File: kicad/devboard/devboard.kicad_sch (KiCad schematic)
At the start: 35 parts, among them J1 USB_C_Receptacle, J2 Conn_01x04_Socket, J3 Conn_02x03_Top_Bottom, J4 Conn_02x02_Top_Bottom, U1 LM3940, U2 CH340G, U3 STM32G030K8Tx, Y1 12 MHz, Y2 8 MHz

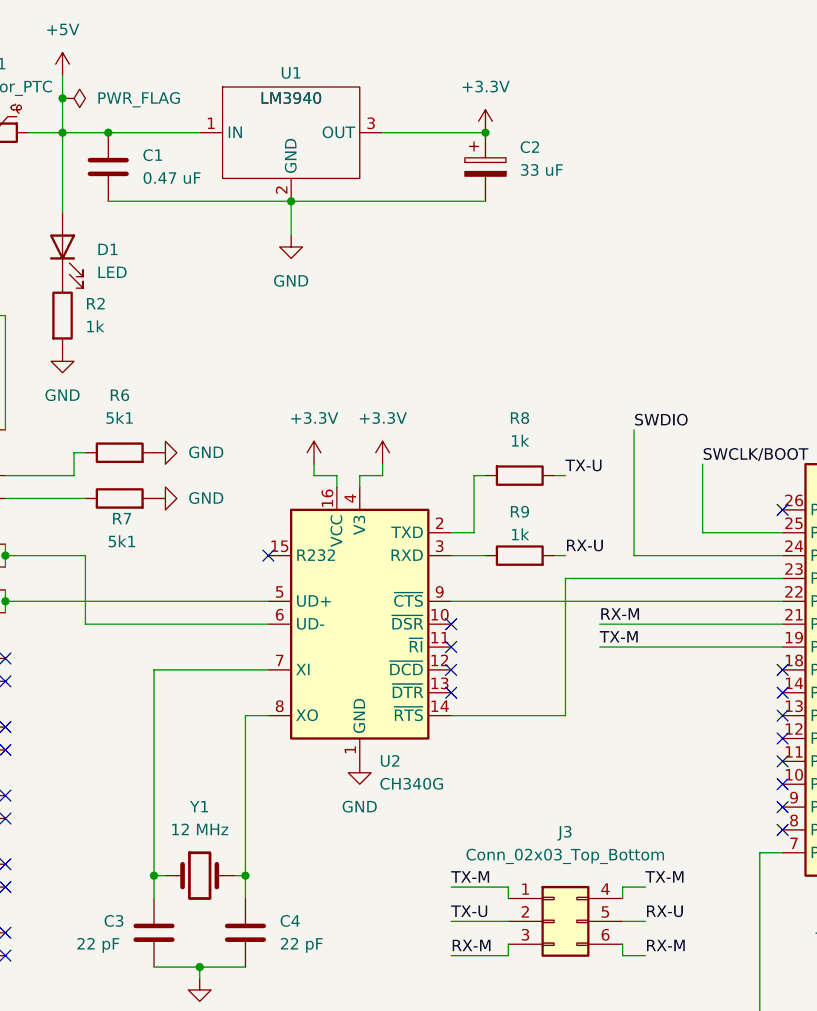
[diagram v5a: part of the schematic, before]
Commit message: updated footprints for Y1, C2
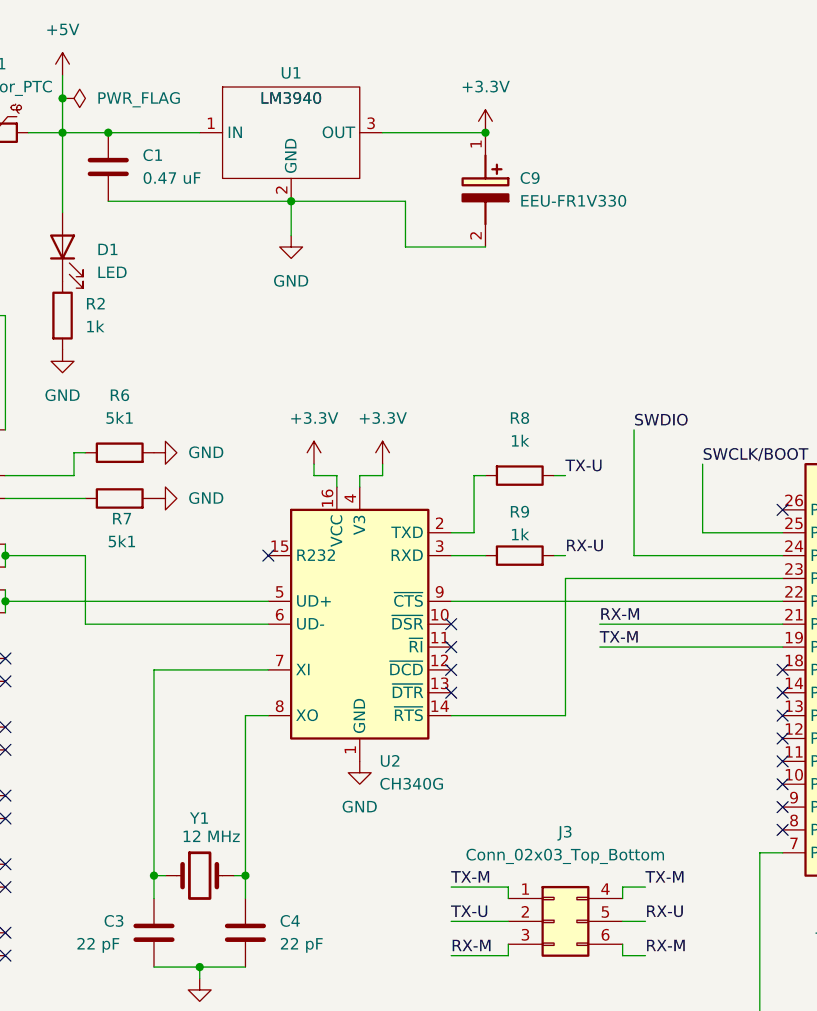
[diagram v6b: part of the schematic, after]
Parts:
- removed C2: 33 uF, Capacitor_SMD:C_0603_1608Metric, symbol Device:C_Polarized
- added C9: EEU-FR1V330, mesonlib:EEU-FR1330, symbol mesonlib:EEU-FR1V330
- Y1: footprint Resistor_SMD:R_0603_1608Metric -> Crystal:Crystal_SMD_HC49-SD
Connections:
- net +3.3V: now also C9.1 (+)
- net GND: now also C9.2 (-)
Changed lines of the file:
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@@
 	)
 	(junction
+		(at 97.79 31.75)
+		(diameter 0)
+		(color 0 0 0 0)
+	)
+	(junction
 		(at 60.96 114.3)
 		(diameter 0)
@@
 	)
 	(junction
-		(at 97.79 31.75)
-		(diameter 0)
-		(color 0 0 0 0)
-	)
-	(junction
 		(at 71.12 114.3)
 		(diameter 0)
@@
 	(wire
 		(pts
+			(xy 88.9 44.45) (xy 88.9 39.37)
+		)
+		(stroke
+			(width 0)
+			(type default)
+		)
+	)
+	(wire
+		(pts
 			(xy 66.04 124.46) (xy 71.12 124.46)
 		)
@@
 	(wire
 		(pts
+			(xy 97.79 44.45) (xy 88.9 44.45)
+		)
+		(stroke
+			(width 0)
+			(type default)
+		)
+	)
+	(wire
+		(pts
 			(xy 78.74 69.85) (xy 81.28 69.85)
 		)
@@
 	(wire
 		(pts
-			(xy 76.2 39.37) (xy 97.79 39.37)
+			(xy 231.14 101.6) (xy 237.49 101.6)
 		)
 		(stroke
@@
 	(wire
 		(pts
-			(xy 231.14 101.6) (xy 237.49 101.6)
+			(xy 39.37 31.75) (xy 39.37 52.07)
 		)
 		(stroke
@@
 	(wire
 		(pts
-			(xy 39.37 31.75) (xy 39.37 52.07)
+			(xy 44.45 82.55) (xy 44.45 83.82)
 		)
 		(stroke
@@
 	(wire
 		(pts
-			(xy 44.45 82.55) (xy 44.45 83.82)
+			(xy 55.88 39.37) (xy 76.2 39.37)
 		)
 		(stroke
@@
 	(wire
 		(pts
-			(xy 55.88 39.37) (xy 76.2 39.37)
+			(xy 50.8 31.75) (xy 50.8 40.64)
 		)
 		(stroke
@@
 	(wire
 		(pts
-			(xy 50.8 31.75) (xy 50.8 40.64)
+			(xy 60.96 114.3) (xy 62.23 114.3)
 		)
 		(stroke
@@
 	(wire
 		(pts
-			(xy 60.96 114.3) (xy 62.23 114.3)
+			(xy 143.51 116.84) (xy 143.51 120.65)
 		)
 		(stroke
@@
 	(wire
 		(pts
-			(xy 143.51 116.84) (xy 143.51 120.65)
+			(xy 76.2 39.37) (xy 88.9 39.37)
 		)
 		(stroke
@@
 	)
 	(symbol
-		(lib_id "Device:C_Polarized")
-		(at 97.79 35.56 0)
-		(unit 1)
-		(exclude_from_sim no)
-		(in_bom yes)
-		(on_board yes)
-		(dnp no)
-		(fields_autoplaced yes)
-		(property "Reference" "C2"
-			(at 101.6 33.4009 0)
-			(effects
-				(font
-					(size 1.27 1.27)
-				)
-				(justify left)
-			)
-		)
-		(property "Value" "33 uF"
-			(at 101.6 35.9409 0)
-			(effects
-				(font
-					(size 1.27 1.27)
-				)
-				(justify left)
-			)
-		)
-		(property "Footprint" "Capacitor_SMD:C_0603_1608Metric"
-			(at 98.7552 39.37 0)
-			(effects
-				(font
-					(size 1.27 1.27)
-				)
-				(hide yes)
-			)
-		)
-		(property "Datasheet" "~"
-			(at 97.79 35.56 0)
-			(effects
-				(font
-					(size 1.27 1.27)
-				)
-				(hide yes)
-			)
-		)
-		(property "Description" "Polarized capacitor"
-			(at 97.79 35.56 0)
-			(effects
-				(font
-					(size 1.27 1.27)
-				)
-				(hide yes)
-			)
-		)
-		(pin "1"
-		)
-		(pin "2"
-		)
-		(instances
-			(project "devboard"
-				(path "/c3bd2aeb-acec-4e93-ab92-7a030f22ab8b"
-					(reference "C2")
-					(unit 1)
-				)
-			)
-		)
-	)
-	(symbol
 		(lib_id "power:PWR_FLAG")
 		(at 50.8 27.94 270)
@@
 		(on_board yes)
 		(dnp no)
-		(fields_autoplaced yes)
 		(property "Reference" "Y1"
-			(at 66.04 106.68 0)
+			(at 66.04 107.95 0)
 			(effects
 				(font
@@
 		)
 		(property "Value" "12 MHz	"
-			(at 66.04 109.22 0)
+			(at 67.31 109.982 0)
 			(effects
 				(font
@@
 			)
 		)
-		(property "Footprint" "Resistor_SMD:R_0603_1608Metric"
+		(property "Footprint" "Crystal:Crystal_SMD_HC49-SD"
 			(at 66.04 114.3 0)
 			(effects
@@
 					(unit 1)
 				)
+			)
+		)
+	)
+	(symbol
+		(lib_id "mesonlib:EEU-FR1V330")
+		(at 97.79 31.75 270)
+		(unit 1)
+		(exclude_from_sim no)
+		(in_bom yes)
+		(on_board yes)
+		(dnp no)
+		(fields_autoplaced yes)
+		(property "Reference" "C9"
+			(at 101.6 36.8299 90)
+			(effects
+				(font
+					(size 1.27 1.27)
+				)
+				(justify left)
+			)
+		)
+		(property "Value" "EEU-FR1V330"
+			(at 101.6 39.3699 90)
+			(effects
+				(font
+					(size 1.27 1.27)
+				)
+				(justify left)
+			)
+		)
+		(property "Footprint" "mesonlib:EEU-FR1330"
+			(at 1.6 40.64 0)
+			(effects
+				(font
+					(size 1.27 1.27)
+				)
+				(justify left top)
+				(hide yes)
+			)
+		)
+		(property "Datasheet" "http://industrial.panasonic.com/cdbs/www-data/pdf/RDF0000/ABA0000C1259.pdf"
+			(at -98.4 40.64 0)
+			(effects
+				(font
+					(size 1.27 1.27)
+				)
+				(justify left top)
+				(hide yes)
+			)
+		)
+		(property "Description" "Aluminium Electrolytic Capacitor, Radial Lead Type, 105C,  33UF 20% 35V RADIAL"
+			(at 97.79 31.75 0)
+			(effects
+				(font
+					(size 1.27 1.27)
+				)
+				(hide yes)
+			)
+		)
+		(property "Height" "12.5"
+			(at -298.4 40.64 0)
+			(effects
+				(font
+					(size 1.27 1.27)
+				)
+				(justify left top)
+				(hide yes)
+			)
+		)
+		(property "Mouser Part Number" "667-EEU-FR1V330"
+			(at -398.4 40.64 0)
+			(effects
+				(font
+					(size 1.27 1.27)
+				)
+				(justify left top)
+				(hide yes)
+			)
+		)
+		(property "Mouser Price/Stock" "https://www.mouser.co.uk/ProductDetail/Panasonic/EEU-FR1V330?qs=ob%252BdNz2%252BYEhHeC0uCpfxxQ%3D%3D"
+			(at -498.4 40.64 0)
+			(effects
+				(font
+					(size 1.27 1.27)
+				)
+				(justify left top)
+				(hide yes)
+			)
+		)
+		(property "Manufacturer_Name" "Panasonic"
+			(at -598.4 40.64 0)
+			(effects
+				(font
+					(size 1.27 1.27)
+				)
+				(justify left top)
+				(hide yes)
+			)
+		)
+		(property "Manufacturer_Part_Number" "EEU-FR1V330"
+			(at -698.4 40.64 0)
+			(effects
+				(font
+					(size 1.27 1.27)
+				)
+				(justify left top)
+				(hide yes)
+			)
+		)
+		(pin "1"
+		)
+		(pin "2"
+		)
+		(instances
+			(project "devboard"
+				(path "/c3bd2aeb-acec-4e93-ab92-7a030f22ab8b"
+					(reference "C9")
+					(unit 1)
+				)

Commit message: All footprints done?
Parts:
- TH1: footprint (none) -> mesonlib:Eaton PTS120616V025
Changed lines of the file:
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@@
 			)
 		)
-		(property "Footprint" ""
+		(property "Footprint" "mesonlib:Eaton PTS120616V025"
 			(at 38.1 33.02 0)
 			(effects

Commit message: fixed footprint for crystal
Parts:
- Y1: footprint Crystal:Crystal_SMD_HC49-SD -> Crystal:Crystal_HC49-4H_Vertical
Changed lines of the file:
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@@
 			)
 		)
-		(property "Footprint" "Crystal:Crystal_SMD_HC49-SD"
+		(property "Footprint" "Crystal:Crystal_HC49-4H_Vertical"
 			(at 66.04 114.3 0)
 			(effects
